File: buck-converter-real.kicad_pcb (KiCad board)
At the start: 4 copper layers, 64 x 64 mm, 114 parts, among them J1 Conn_01x02_Pin, J1 USB_C_Receptacle_USB2.0_16P, J10 I2C1, J11 SWD, J12 Conn_01x04, J13 Conn_01x15, J14 Conn_01x04, J15 Conn_01x06, J6 DM3CS-SF, J8 I2C1, J9 SWD, Q1 CSD18540Q5B - 60-V, U1 AP2112K-3.3 (3V3 LDO), U10 TLV75733PDRV, U2 CH32V203K8T6, U4 LMR51610YDBVR, U5 LM5109BMA/NOPB, U6 TPT482-VS2R, U7 TCAN3414DDFR, U8 TPS61022, Y1 8MHz 20pF

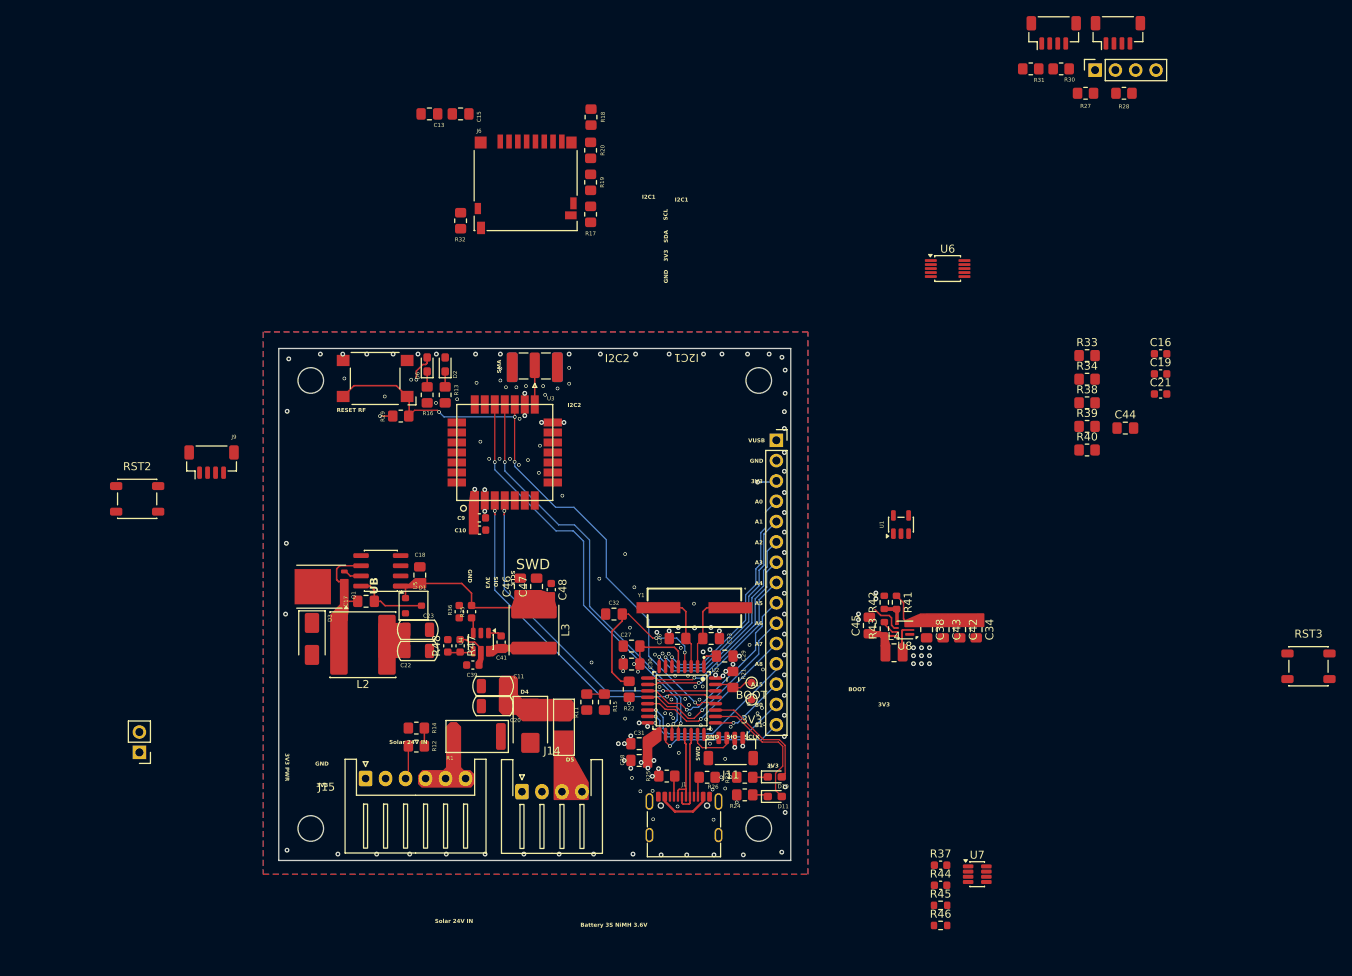
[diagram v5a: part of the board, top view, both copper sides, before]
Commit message: Swap to 12V LDO
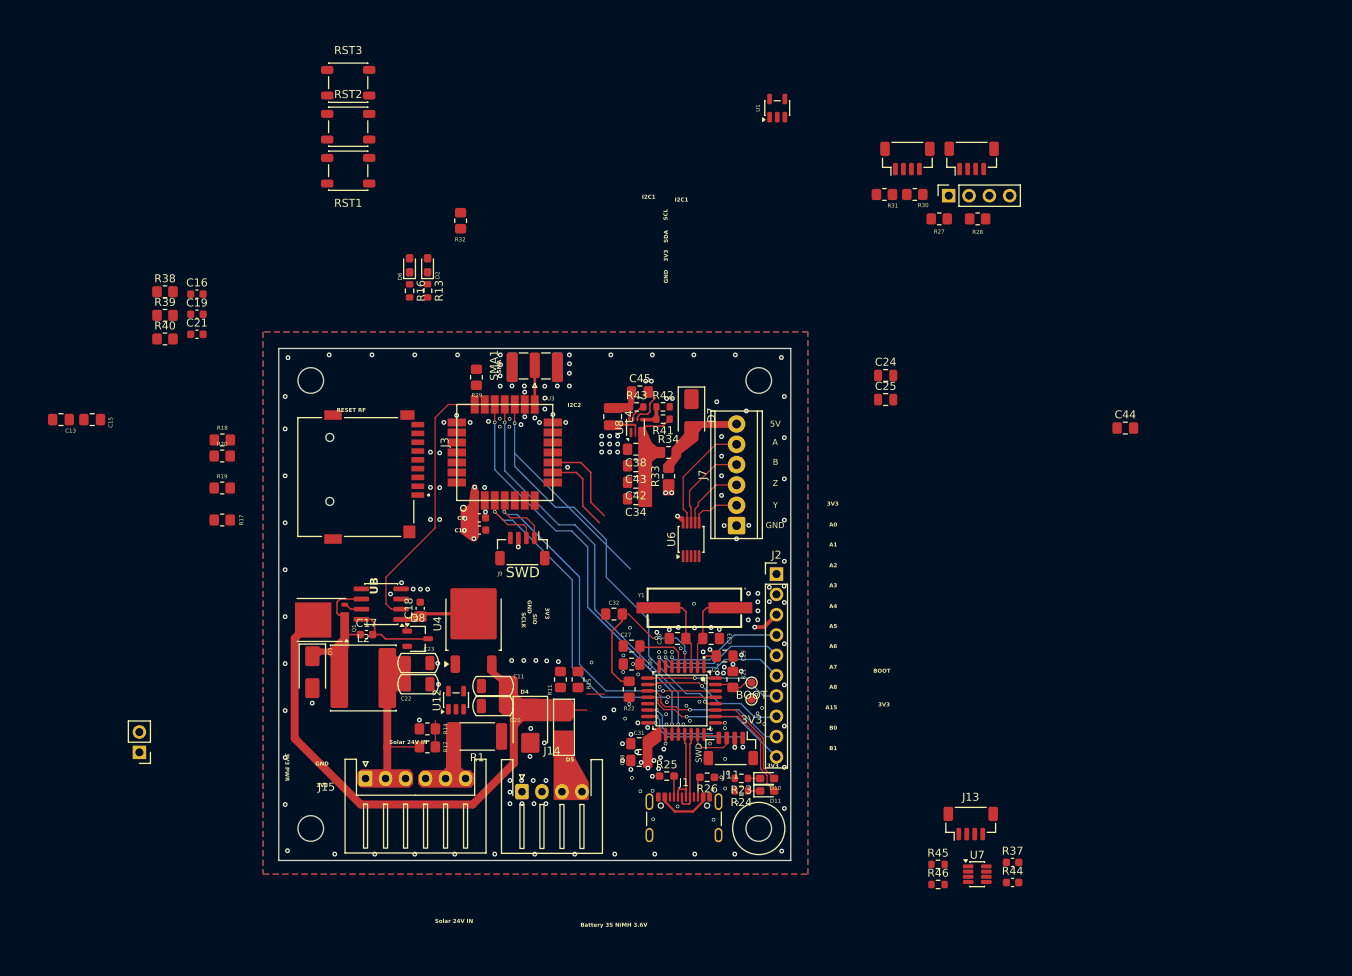
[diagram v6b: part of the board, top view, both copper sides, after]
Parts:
- removed C39: 2.2uF, Capacitor_SMD:C_0603_1608Metric
- removed C41, C48: 100nF, Capacitor_SMD:C_0603_1608Metric
- removed C46, C47: 22uF 10V X7R/X5R 0805, Capacitor_SMD:C_0805_2012Metric_Pad1.18x1.45mm_HandSolder
- removed D1: BAT54C, PCM_Package_TO_SOT_SMD_AKL:SOT-23
- removed J6: DM3CS-SF, Connector_Card:microSD_HC_Hirose_DM3D-SF
- removed L3: 68u, Inductor_SMD:L_Chilisin_BWVS00606020
- removed R35: 309k, Capacitor_SMD:C_0603_1608Metric
- removed R36: 22.1k, Capacitor_SMD:C_0603_1608Metric
- removed R47: 1.5m, Capacitor_SMD:C_0603_1608Metric
- removed R48: 100k, Capacitor_SMD:C_0603_1608Metric
- removed SMA-915/433MHz1: SMA-ANT, Connector_Coaxial:SMA_Samtec_SMA-J-P-H-ST-EM1_EdgeMount
- added C24: 1u 100V, Capacitor_SMD:C_0805_2012Metric, F.Cu at (143.9, 71.4)
- added C25: 10u 16V, Capacitor_SMD:C_0805_2012Metric, F.Cu at (143.9, 74.4)
- added D7: SMAJ5.0CA clamp@9.2V, Diode_SMD:D_SMA, F.Cu at (119.6, 76.3)
- added D8: BAT54C, Package_TO_SOT_SMD:TSOT-23, F.Cu at (85.4, 104.3)
- added J2: Conn_01x10, Connector_PinHeader_2.54mm:PinHeader_1x10_P2.54mm_Vertical, F.Cu at (130.2, 96.2)
- added J3: MSD-1-A, buck-forest:CUI_MSD-1-A, F.Cu at (77.6, 84.1)
- added J7: Conn_01x06, TerminalBlock_Phoenix:TerminalBlock_Phoenix_MPT-0,5-6-2.54_1x06_P2.54mm_Horizontal, F.Cu at (125.2, 90.1)
- added SMA1: ANT-SMA, Connector_Coaxial:SMA_Samtec_SMA-J-P-H-ST-EM1_EdgeMount, F.Cu at (100.0, 70.1)
- added U12: INA180A1, Package_TO_SOT_SMD:SOT-23-5, F.Cu at (90.2, 112.0)
- C17, C18: footprint Capacitor_SMD:C_0805_2012Metric_Pad1.18x1.45mm_HandSolder -> Capacitor_SMD:C_0603_1608Metric
- D4: value SMBJ43A - 43VWM 69.4VC -> SMBJ54A
- J1: footprint Connector_USB:USB_C_Receptacle_G-Switch_GT-USB-7010ASV -> Connector_USB:USB_C_Receptacle_GCT_USB4105-xx-A_16P_TopMnt_Horizontal
- J13: value Conn_01x15 -> CAN; footprint Connector_PinSocket_2.54mm:PinSocket_1x15_P2.54mm_Vertical -> Connector_JST:JST_SH_BM04B-SRSS-TB_1x04-1MP_P1.00mm_Vertical
- L2: value 10uH ±20% 18mΩ Molded -> 10uH 18mOhm
- R1: value Shunt 50m Ohm -> Shunt 50m Ohm 2512; footprint PCM_Resistor_SMD_AKL:R_2512_6332Metric -> Resistor_SMD:R_2512_6332Metric_Pad1.40x3.35mm_HandSolder
- R11: value 10K -> 100K
- R13, R16, R23, R24: footprint Resistor_SMD:R_0805_2012Metric_Pad1.20x1.40mm_HandSolder -> Resistor_SMD:R_0603_1608Metric
- R15: value 1.5K -> 10k
- R25, R26: footprint Resistor_SMD:R_0805_2012Metric_Pad1.20x1.40mm_HandSolder -> Resistor_SMD:R_0603_1608Metric_Pad0.98x0.95mm_HandSolder
- R30, R31: value 4.7K -> 4.7K 0805
- R38, R39, R40: value 0 -> TBD
- RST1: footprint Button_Switch_SMD:SW_SPST_Omron_B3FS-100xP -> Button_Switch_SMD:SW_SPST_PTS647_Sx38
- U4: value LMR51610YDBVR -> ZXTR2012K-13 12V@50mA vin<100V; footprint Package_TO_SOT_SMD:SOT-23-6 -> Package_TO_SOT_SMD:TO-252-2
- U5: value LM5109BMA/NOPB -> LM5109BMA
- moved RST3 140.5 mm to (76.7, 34.8)
- moved C16 120.7 mm to (57.8, 61.2)
- moved C19 120.7 mm to (57.8, 63.7)
- moved C21 120.7 mm to (57.8, 66.2)
- moved R38 116.1 mm to (53.8, 60.9)
- moved R39 116.1 mm to (53.8, 63.9)
- moved R40 116.1 mm to (53.8, 66.8)
- moved R18 61.2 mm to (61.0, 79.4), turned to 180 degrees
- moved C13 59.8 mm to (40.8, 76.9)
- moved C15 59.8 mm to (44.7, 76.9)
- moved R17 59.8 mm to (60.9, 89.4), turned to 180 degrees
- moved R19 59.8 mm to (60.9, 85.4), turned to 180 degrees
- moved R20 59.8 mm to (60.9, 81.4), turned to 0 degrees
- moved R33 54.4 mm to (116.7, 84.0), turned to 90 degrees
- moved U1 54.3 mm to (130.3, 38.0)
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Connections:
- net Net-(U7-RXD) renamed /CAN_RX
- net Net-(U7-TXD) renamed /CAN_TX
- C17 pad 1: Net-(D3-K) -> /HS
- C18 pad 1: /12V-buck -> /12V
- D3 pad 1: Net-(D3-K) -> /HS
- J10 pad MP: unconnected-(J10-Shield-PadMP)_1 -> (no net)
- J13 pad 1: VBUS -> GND
- J13 pad 2: GND -> /CAN_LOW
- J13 pad 3: +3.3V -> /CAN_HI
- J13 pad 4: Net-(J13-Pin_4) -> +3.3V
- J15 pad 4: /BAT_ISENSE -> Net-(J15-Pin_4)
- J15 pad 5: /BAT_ISENSE -> Net-(J15-Pin_4)
- J15 pad 6: /BAT_ISENSE -> Net-(J15-Pin_4)
- J9 pad 1: GND -> /SWD-WIO-CLK
- J9 pad 2: +3.3V -> /SWD-WIO-IO
- J9 pad 3: /SWD-WIO-IO -> +3.3V
- J9 pad 4: /SWD-WIO-CLK -> GND
- L2 pad 1: +BATT -> /HS
- L2 pad 2: Net-(D3-K) -> +BATT
- Q1 pad 1: Net-(D3-K) -> /HS
- Q1 pad 2: Net-(D3-K) -> /HS
- Q1 pad 3: Net-(D3-K) -> /HS
- R1 pad 2: /BAT_ISENSE -> Net-(J15-Pin_4)
- R37 pad 1: Net-(U7-CANH) -> /CAN_HI
- R44 pad 2: Net-(U7-CANL) -> /CAN_LOW
- U2 pad 10: Net-(J13-Pin_8) -> Net-(J2-Pin_8)
- U2 pad 11: Net-(J13-Pin_9) -> Net-(J2-Pin_9)
- U2 pad 12: Net-(J13-Pin_10) -> Net-(J2-Pin_10)
- U2 pad 13: Net-(J13-Pin_11) -> unconnected-(U2-PA7/ADC7-Pad13)
- U2 pad 14: Net-(J13-Pin_12) -> unconnected-(U2-PB0/ADC8-Pad14)
- U2 pad 15: Net-(J13-Pin_14) -> unconnected-(U2-PB1/ADC9-Pad15)
- U2 pad 18: Net-(J13-Pin_15) -> /CAN_S
- U2 pad 25: Net-(J13-Pin_13) -> /CAN_FAULT
- U2 pad 6: Net-(J13-Pin_4) -> Net-(J2-Pin_4)
- U2 pad 7: Net-(J13-Pin_5) -> Net-(J2-Pin_5)
- U2 pad 8: Net-(J13-Pin_6) -> Net-(J2-Pin_6)
- U2 pad 9: Net-(J13-Pin_7) -> Net-(J2-Pin_7)
- U4 pad 1: Net-(U4-CB) -> GND
- U4 pad 2: GND -> /12V
- U4 pad 3: Net-(U4-FB) -> /Solar In
- U5 pad 1: /12V-buck -> /12V
- U5 pad 6: Net-(D3-K) -> /HS
- U6 pad 6: Net-(J7-Pin_5) -> /RS422_Y
- U6 pad 7: Net-(J7-Pin_4) -> /RS422_Z
- U6 pad 8: Net-(J7-Pin_3) -> /RS422_B
- U6 pad 9: Net-(J7-Pin_2) -> /RS422_A
- U7 pad 5: unconnected-(U7-FAULT-Pad5) -> /CAN_FAULT
- U7 pad 6: Net-(U7-CANL) -> /CAN_LOW
- U7 pad 7: Net-(U7-CANH) -> /CAN_HI
- U7 pad 8: unconnected-(U7-S-Pad8) -> /CAN_S
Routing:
- net /Solar In: track 4.78 -> 59.6 mm
- net /PWM_HI: track 0.65 -> 34.3 mm
- net Net-(J13-Pin_4): track 29.5 -> 0.00 mm, vias 1 -> 0
- net Net-(J13-Pin_5): track 28.4 -> 0.00 mm, vias 1 -> 0
- net Net-(J13-Pin_6): track 27.4 -> 0.00 mm, vias 1 -> 0
- net Net-(J13-Pin_7): track 25.3 -> 0.00 mm, vias 1 -> 0
- net Net-(J13-Pin_9): track 24.5 -> 0.00 mm, vias 1 -> 0
- net Net-(J13-Pin_8): track 23.2 -> 0.00 mm, vias 1 -> 0
- net Net-(J13-Pin_10): track 23.1 -> 0.00 mm, vias 1 -> 0
- net Net-(J13-Pin_12): track 22.2 -> 0.00 mm, vias 1 -> 0
- net Net-(J13-Pin_11): track 21.0 -> 0.00 mm, vias 1 -> 0
- net Net-(J2-Pin_10): track 0.00 -> 19.5 mm, vias 0 -> 1
- net Net-(J13-Pin_14): track 19.5 -> 0.00 mm, vias 1 -> 0
- net /12V-buck: track 19.0 -> 0.00 mm
- net Net-(J2-Pin_9): track 0.00 -> 18.9 mm, vias 0 -> 1
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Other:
- board text added: "100kHz PWM"
- board text added: "5V"
- board text added: "A"
- board text added: "B"
- board text added: "COATL Forest Sensor Platform V2"
- board text added: "Minimum via stitching distance"
- board text added: "Y"
- board text added: "Z"
- board text removed: "COATL Forest Sensor Platform V1"

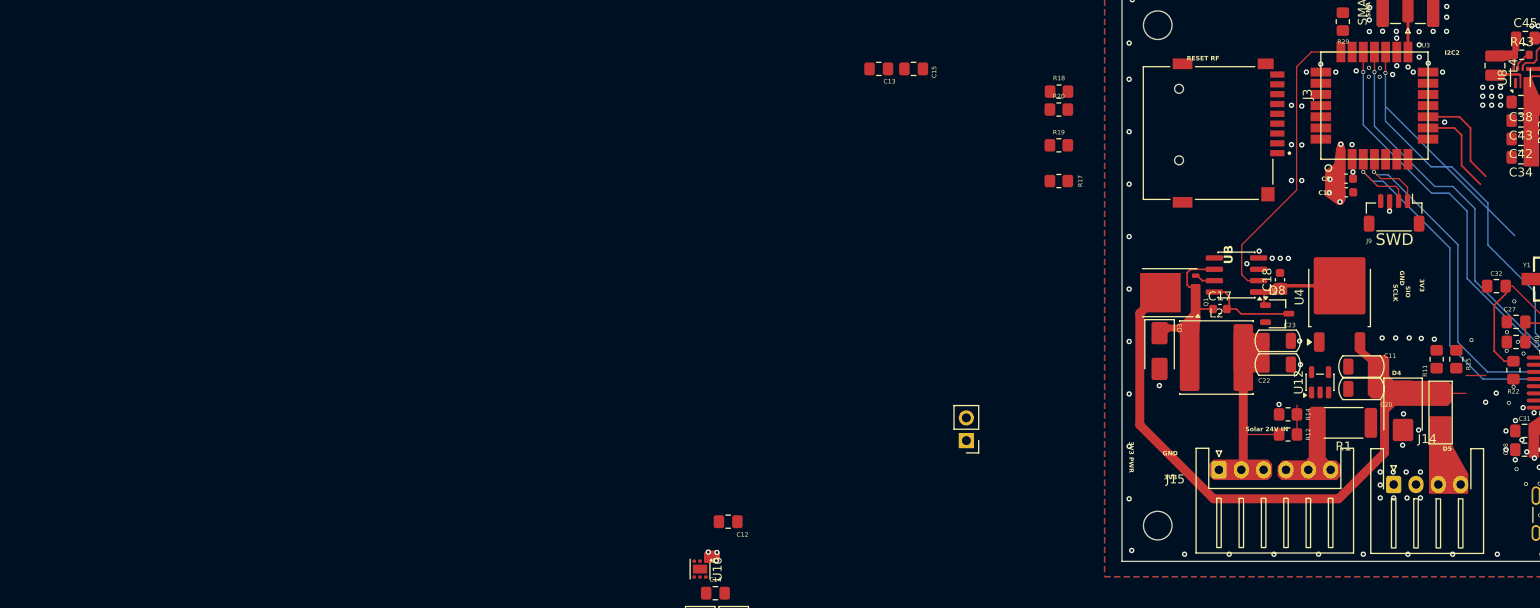
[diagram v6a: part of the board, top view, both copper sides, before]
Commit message: Swap from bat54 to ss510 for buck driver
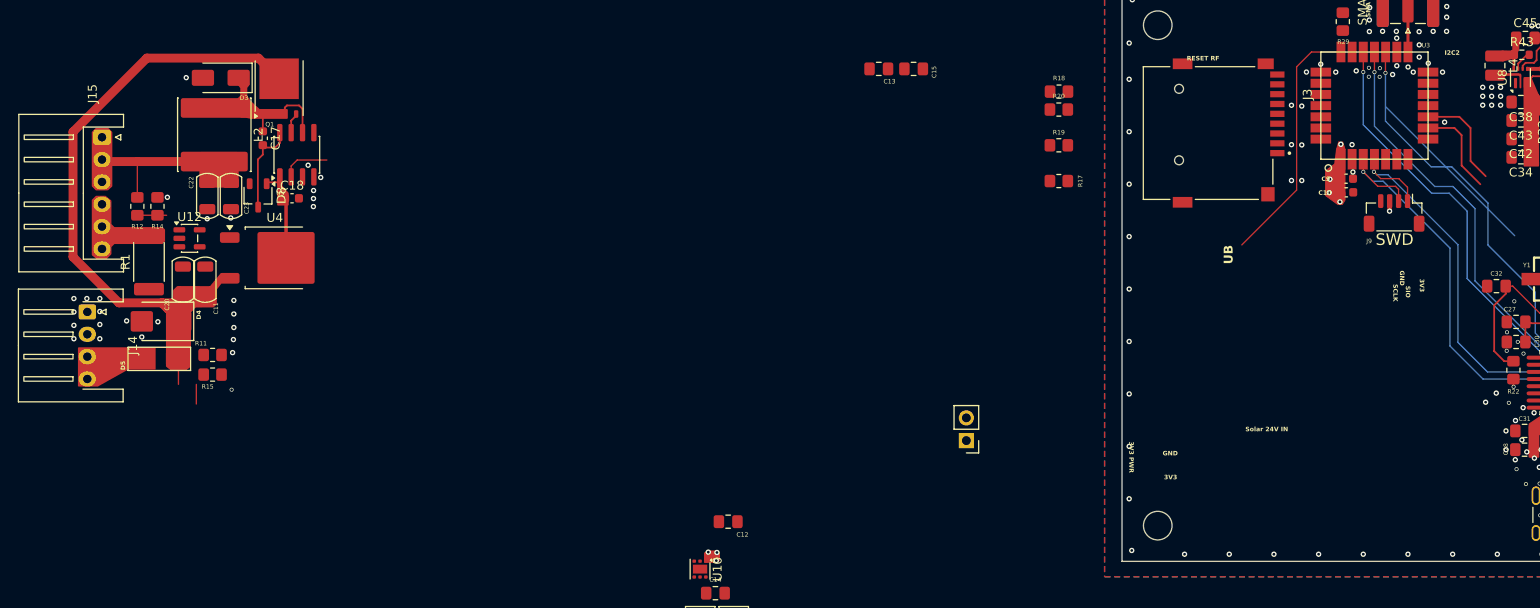
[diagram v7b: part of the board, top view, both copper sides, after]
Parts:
- moved J14 147.5 mm to (-47.8, 104.1), turned to -90 degrees
- moved D5 143.5 mm to (-39.7, 109.3), turned to 180 degrees
- moved D4 139.3 mm to (-39.5, 105.1), turned to 180 degrees
- moved R15 139.2 mm to (-33.8, 111.1), turned to 180 degrees
- moved R11 137.0 mm to (-33.8, 108.9), turned to 0 degrees
- moved R1 134.9 mm to (-40.9, 98.5), turned to 90 degrees
- moved C20 132.5 mm to (-37.1, 100.5), turned to 90 degrees
- moved R12 131.3 mm to (-42.2, 92.3), turned to -90 degrees
- moved J15 130.4 mm to (-46.1, 84.5), turned to -90 degrees
- moved C11 129.8 mm to (-34.6, 100.5), turned to 90 degrees
- moved R14 128.6 mm to (-39.9, 92.3), turned to 90 degrees
- moved U12 127.5 mm to (-36.4, 95.8), turned to 0 degrees
- moved C22 121.3 mm to (-34.4, 91.1), turned to -90 degrees
- moved U4 119.2 mm to (-26.8, 98.0), turned to 0 degrees
- moved C23 118.2 mm to (-31.7, 91.1), turned to -90 degrees
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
